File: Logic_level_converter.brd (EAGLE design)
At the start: 49.2 x 48.2 mm, 9 parts, among them Q1 2N7000, Q2 2N7000

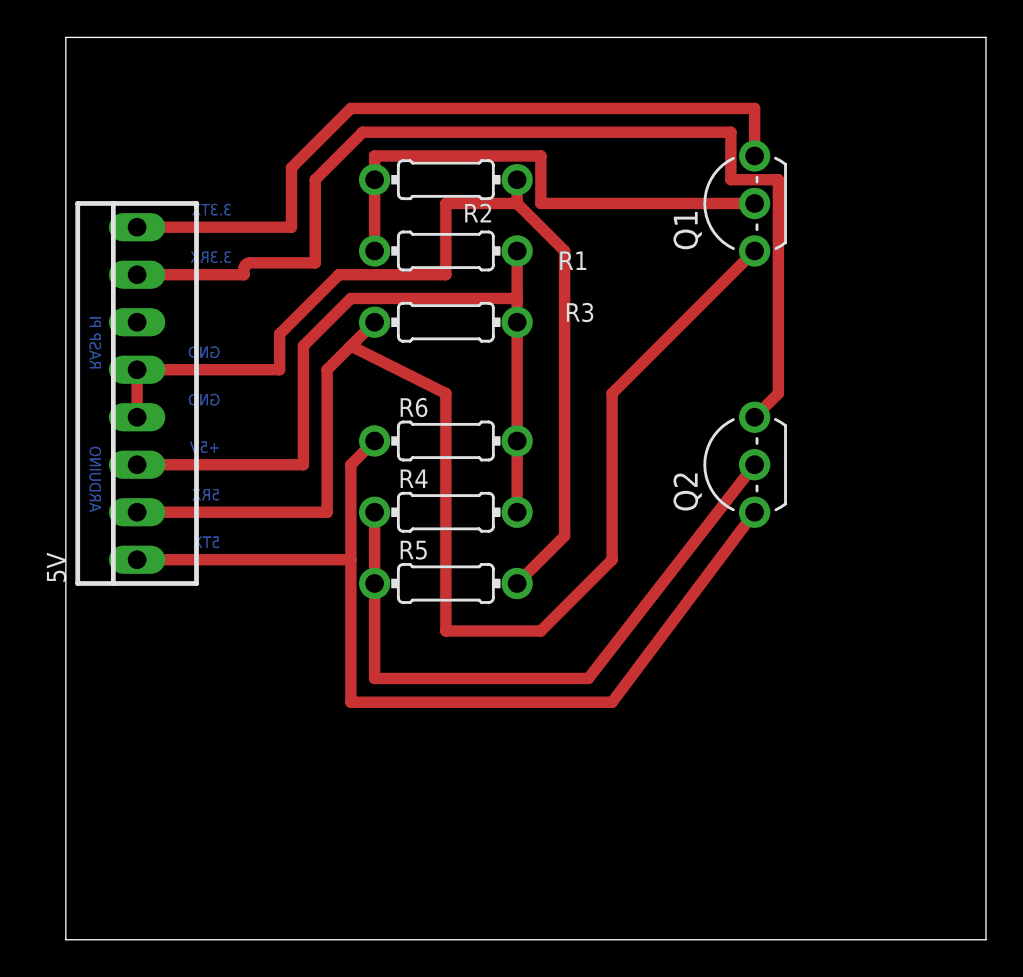
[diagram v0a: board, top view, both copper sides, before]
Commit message: pulled down all the eagle files on github.  histogram.py generates a histogram of the frequency of their usage.  You can make all the boards on github with ~1460 unique parts
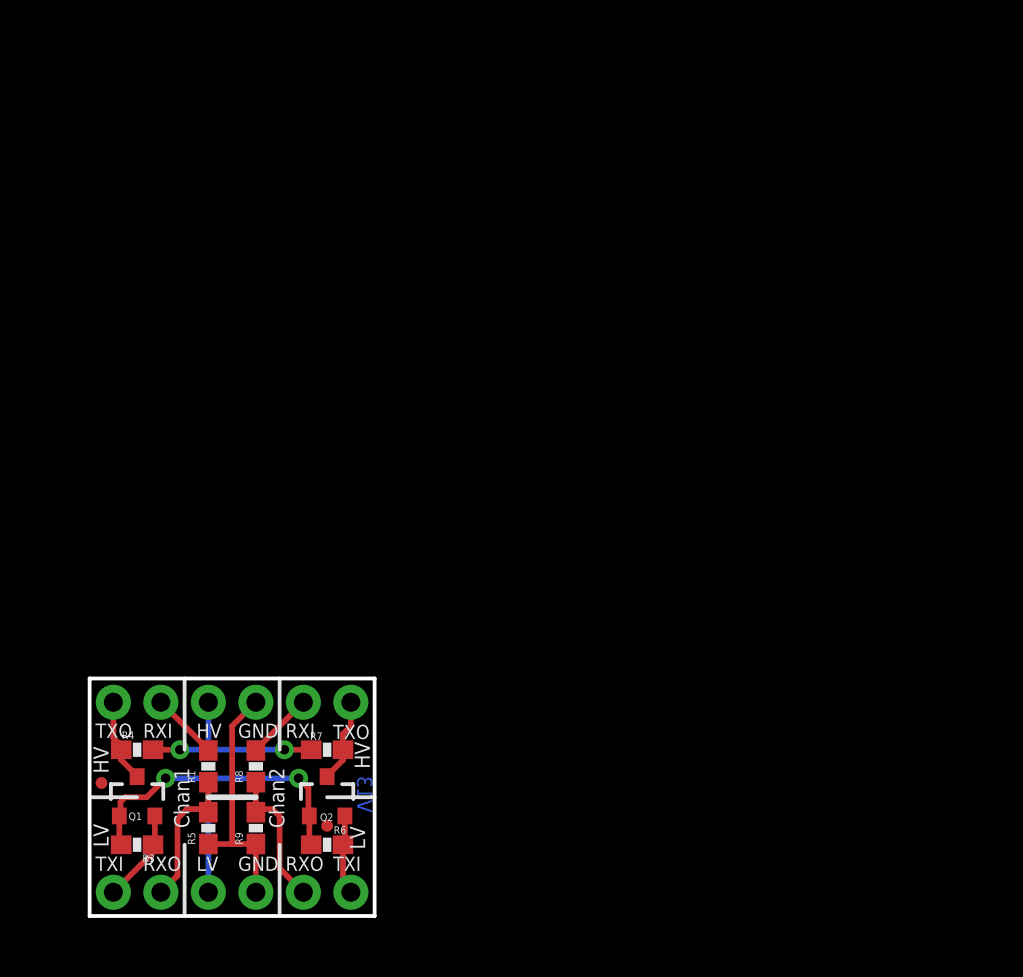
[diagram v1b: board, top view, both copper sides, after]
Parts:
- removed 5V: (no value), con-molex:22-23-2081
- removed R2: 10k, eagle-ltspice:0204/7
- added CC_TEXT1: CREATIVE_COMMONS, SparkFun-Aesthetics:CREATIVE_COMMONS
- added JP1, JP2: (no value), SparkFun:1X06
- added JP3, JP4: FIDUCIALUFIDUCIAL, SparkFun:MICRO-FIDUCIAL
- added JP5: LOGO-SFENW2, SparkFun-Aesthetics:SFE-NEW-WEB
- added R7, R8: 10K, SparkFun:0603-RES
- added R9: 20K, SparkFun:0603-RES
- added U$1: LOGO-SFESK, SparkFun:SFE-LOGO-FLAME
- added U$2: OSHW-LOGOS, SparkFun-Aesthetics:OSHW-LOGO-S
- Q1, Q2: value 2N7000 -> BSS138; device maxim:TO92- -> SparkFun:SOT23-3
- R1, R4: value 4.7k -> 10K; device eagle-ltspice:0204/7 -> SparkFun:0603-RES
- R3, R6: value 10k -> 10K; device eagle-ltspice:0204/7 -> SparkFun:0603-RES
- R5: value 10k -> 20K; device eagle-ltspice:0204/7 -> SparkFun:0603-RES
- moved Q1 45.8 mm to (2.54, 6.35), turned to 0 degrees
- moved R3 32.5 mm to (2.54, 3.81)
- moved R1 30.3 mm to (6.35, 8.00), turned to 90 degrees
- moved Q2 29.0 mm to (12.7, 6.35), turned to 0 degrees
- moved R6 22.5 mm to (12.7, 3.81)
- moved R4 20.8 mm to (2.54, 8.89), turned to 180 degrees
- moved R5 18.2 mm to (6.35, 4.70), turned to 90 degrees
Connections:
- removed net N$6: 5V.4, 5V.5, R2.1, R5.2
- removed net S$1: Q1.2, R1.2, R2.2
- removed net S$2: 5V.8, Q1.3
- removed net S$3: 5V.2, Q1.1, R3.1
- removed net S$5: Q2.2, R4.1, R5.1
- removed net S$6: 5V.3, R1.1, R3.2, R4.2, R6.2
- removed net S$7: 5V.1, Q2.1, R6.1
- removed net S$8: 5V.7, Q2.3
- new net GND: JP1.3, JP2.4, R5.1, R9.1
- new net HV: JP2.3, R4.1, R7.1
- new net LV: JP1.4, Q1.1, Q2.1, R3.1, R6.1
- new net RX2_HV: JP2.5, R8.2
- new net RX2_LV: JP1.2, R8.1, R9.2
- new net RX_HV: JP2.2, R1.2
- new net RX_LV: JP1.5, R1.1, R5.2
- new net TX2_HV: JP2.6, Q2.3, R7.2
- new net TX2_LV: JP1.1, Q2.2, R6.2
- new net TX_HV: JP2.1, Q1.3, R4.2
- new net TX_LV: JP1.6, Q1.2, R3.2
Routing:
- net S$3: track 69.9 -> 0.00 mm
- net S$8: track 56.0 -> 0.00 mm
- net N$6: track 53.6 -> 0.00 mm
- net S$7: track 52.6 -> 0.00 mm
- net S$6: track 41.7 -> 0.00 mm
- net S$2: track 40.1 -> 0.00 mm
- net S$5: track 34.8 -> 0.00 mm
- net S$1: track 27.9 -> 0.00 mm
- net LV: track 0.00 -> 22.9 mm, vias 0 -> 2
- net GND: track 0.00 -> 13.2 mm
- net HV: track 0.00 -> 11.0 mm, vias 0 -> 2
- net RX_LV: track 0.00 -> 7.93 mm
- net RX2_LV: track 0.00 -> 7.79 mm
- net TX_LV: track 0.00 -> 5.30 mm
- net TX_HV: track 0.00 -> 4.81 mm
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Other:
- board size 49.2 x 48.2 mm -> 15.2 x 12.7 mm
- board text added: "Chan1"
- board text added: "Chan2"
- board text added: "HV"
- board text added: "LV"
- board text added: "Level Converter"
- board text added: "Nathan Seidle"
- board text added: "RXI"
- board text added: "RXO"
- board text added: "Rev V13 by Patrick Alberts"
- board text added: "TXI"
- board text added: "TXO"
- board text added: "V13"
- board text removed: "+5V"
- board text removed: "3.3RX"
- board text removed: "3.3TX"
- board text removed: "5RX"
- board text removed: "5TX"
- board text removed: "ARDUINO"
- board text removed: "RASP PI"
